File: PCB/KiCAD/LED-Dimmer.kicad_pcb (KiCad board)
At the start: 2 copper layers, 31 x 25 mm, 9 parts, among them Q1 BC547, U1 NE555D

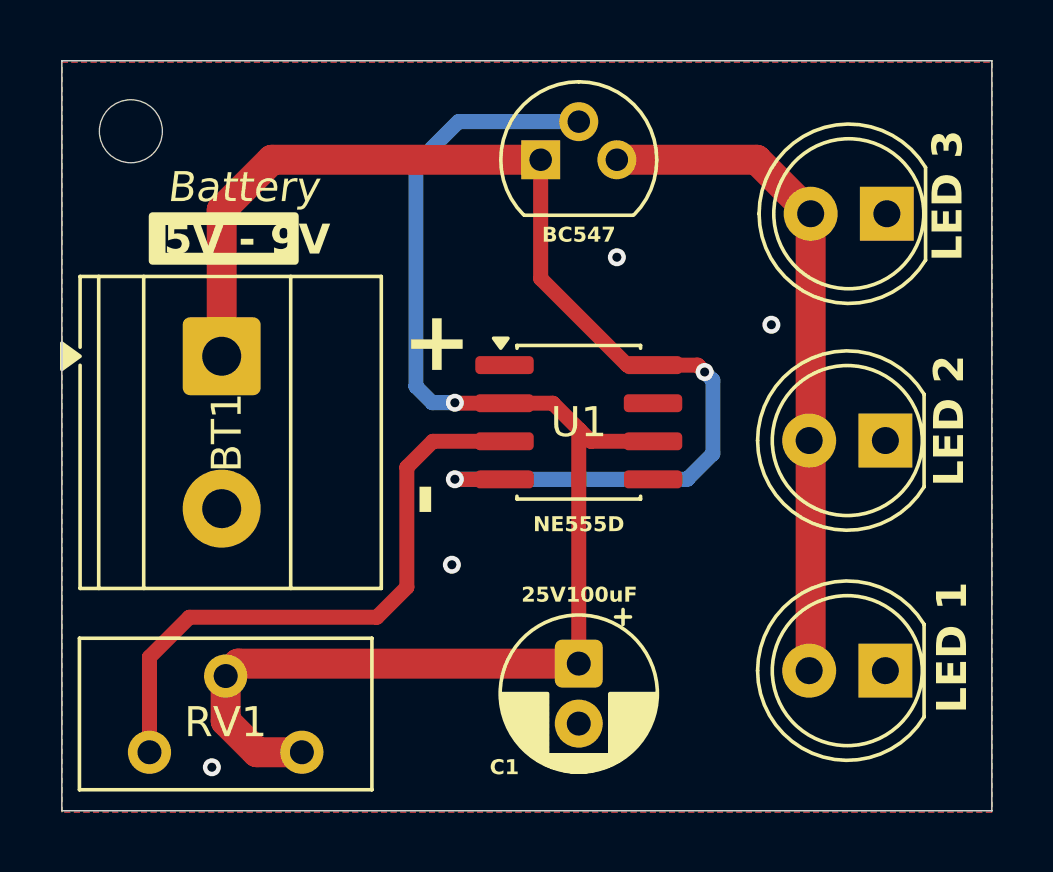
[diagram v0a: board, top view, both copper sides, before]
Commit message: Revise layout
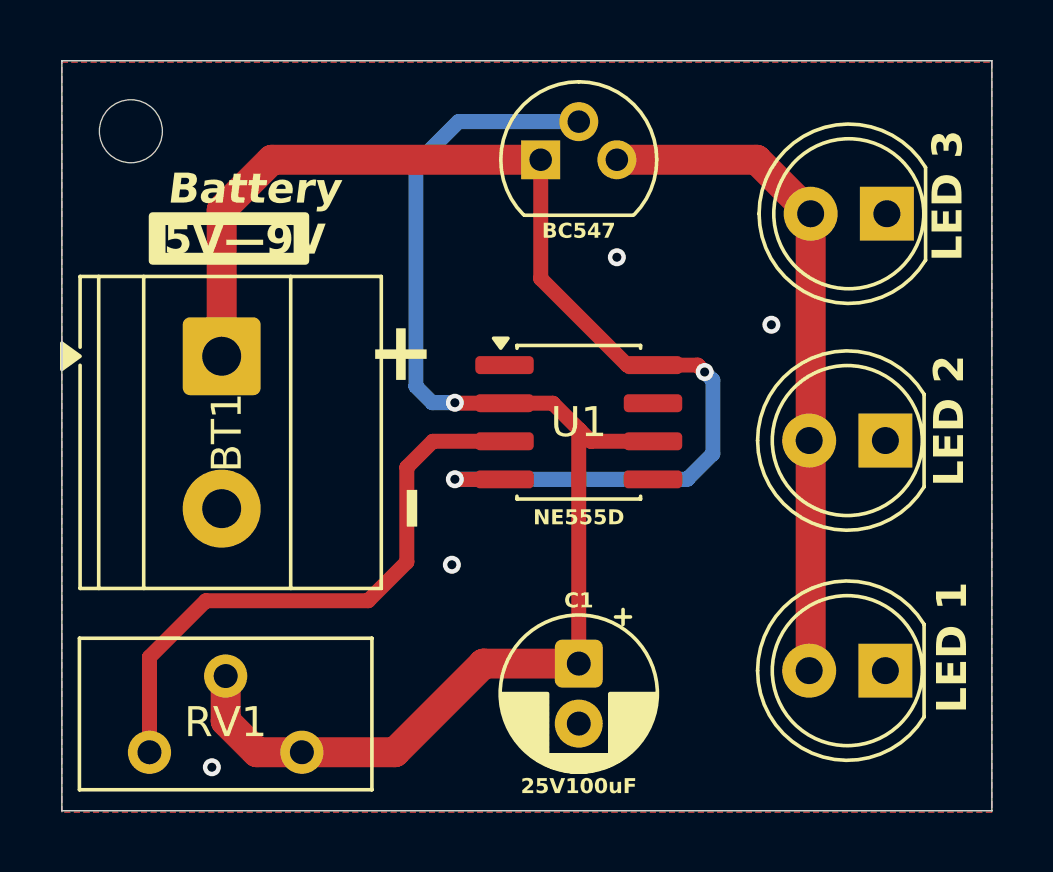
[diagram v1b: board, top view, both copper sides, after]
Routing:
- net /TR: track 46.8 -> 45.3 mm
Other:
- board text added: "5V—9V"
- board text added: "—"
- board text removed: "-"
- board text removed: "5V - 9V"

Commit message: Add resistor
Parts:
- added G***: LOGO, LOGO, B.Cu at (236.7, 85.3)
- added R1: 330, Resistor_THT:R_Axial_DIN0204_L3.6mm_D1.6mm_P7.62mm_Horizontal, F.Cu at (233.4, 74.2)
- moved Q1 4.20 mm to (235.9, 79.5)
- moved U1 1.65 mm to (237.2, 85.7)
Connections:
- Q1 pad 3: Net-(D1-A) -> Net-(Q1-E)
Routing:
- net Net-(Q1-E): track 0.00 -> 9.34 mm
- net +9V: track 40.4 -> 33.8 mm
- net /TR: track 45.3 -> 41.9 mm
- net Net-(U1-Q): track 19.8 -> 18.7 mm
- net Net-(D1-A): track 22.5 -> 21.5 mm
- net GND: vias 4 -> 3
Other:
- outline, holes or cut-outs redrawn
